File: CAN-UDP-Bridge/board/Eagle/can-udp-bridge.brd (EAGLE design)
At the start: 23.8 x 35.5 mm, 15 parts, among them IC2 MCP1703DB, Q1 16M, X1 B4B-ZR

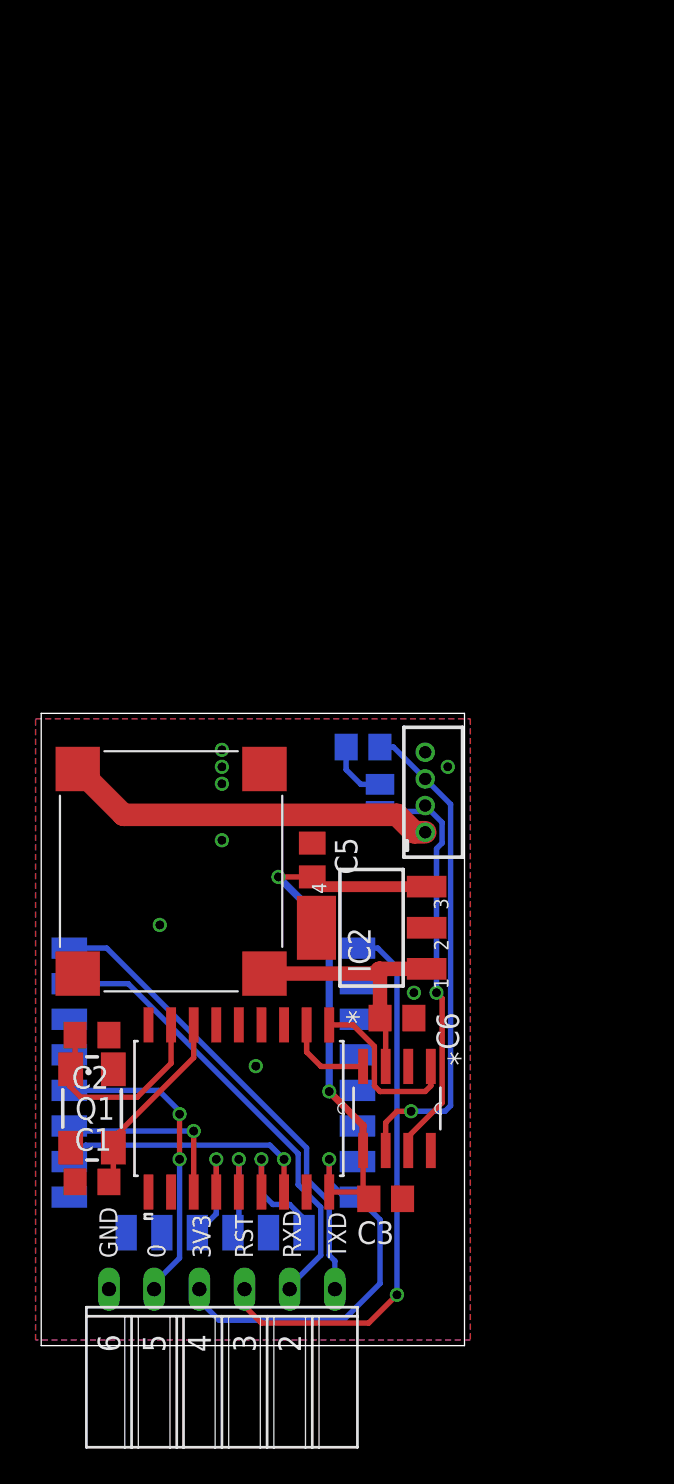
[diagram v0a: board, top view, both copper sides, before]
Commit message: Schnittstelle angepasst an FT232RL.
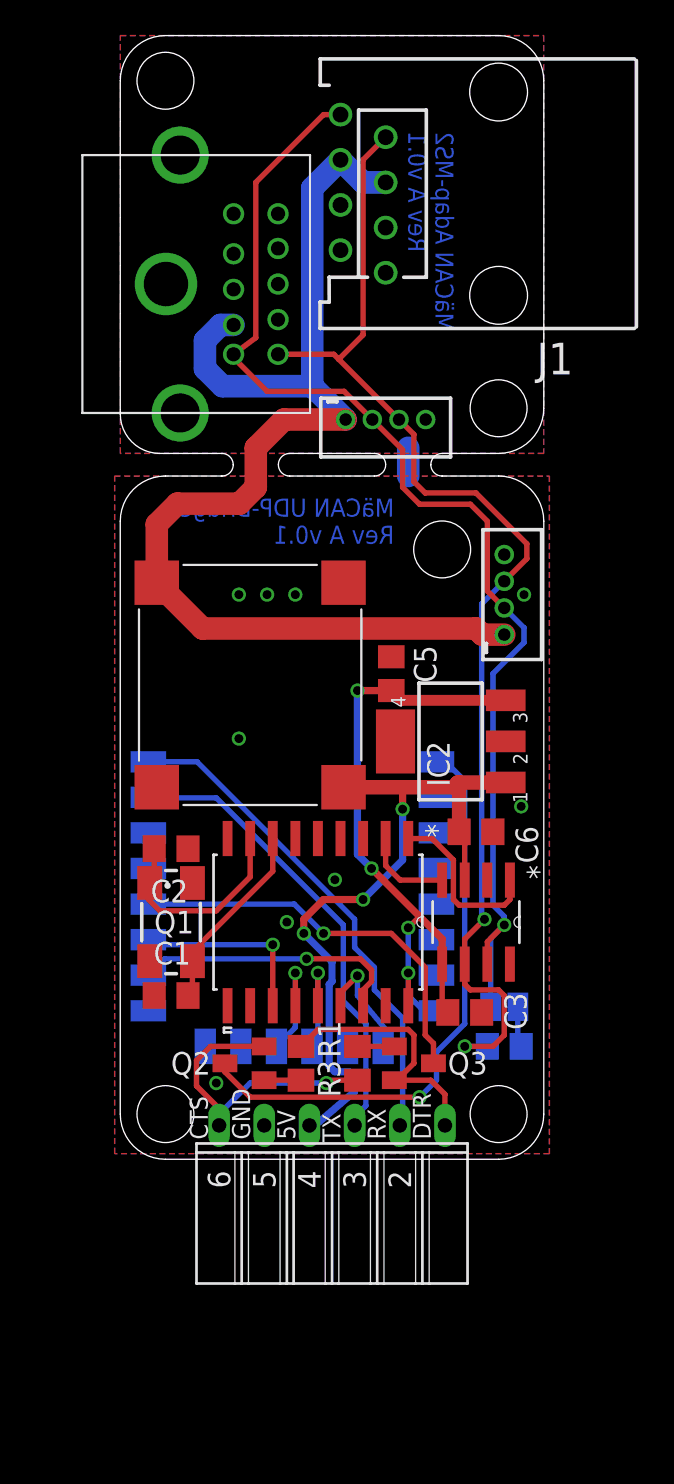
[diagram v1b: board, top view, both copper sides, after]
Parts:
- added J1: (no value), con-amp:215877-7
- added Q2, Q3: (no value), semicon-smd-ipc:SOT23
- added R1, R3: 12k, rcl:R0805
- added U$4: MARKLIN-MD-10, Marklin-Mini-DIN:MARKLIN-MD-10-PRINT
- added X3: B4B-ZR, con-jst:B4B-ZR
- moved R2 18.6 mm to (26.7, 16.8), turned to 180 degrees
- moved CAN-TERM 13.7 mm to (26.7, 19.1), turned to 180 degrees
- moved X1 12.0 mm to (26.7, 42.2)
- moved C2 11.4 mm to (7.94, 27.9)
- moved C3 11.4 mm to (24.4, 18.7)
- moved MDL1 11.4 mm to (22.9, 16.8)
- moved C1 11.4 mm to (7.94, 19.7)
- moved C5 11.4 mm to (20.3, 37.8)
- moved C6 11.4 mm to (25.1, 28.9)
- moved Q1 11.4 mm to (7.94, 23.8)
- moved U$1 11.4 mm to (16.2, 23.8)
- moved U$2 11.4 mm to (25.1, 23.8)
- moved U$3 11.4 mm to (12.4, 37.1)
- moved IC2 11.4 mm to (23.7, 34.0)
- moved PROG 11.1 mm to (17.0, 12.4)
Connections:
- new net DTR: PROG.1, Q3.2, R3.1
- new net N$12: Q2.1, R3.2
- new net N$16: MDL1.16, PROG.2
- new net N$17: MDL1.15, PROG.3
- net +18V: now also J1.5, J1.6, U$4.1, X3.1
- net +3V3: no longer PROG.4
- net +5V: now also PROG.4
- net CAN_H: now also J1.8, U$4.4, X3.2
- net CAN_L: now also J1.7, U$4.8, X3.3
- net GND: now also J1.3, J1.4, PROG.5, U$4.2, U$4.GND1, U$4.GND2, U$4.GND3, X3.4; no longer PROG.6
- net N$10: now also MDL1.12, Q3.3; no longer MDL1.1, PROG.3
- net N$11: now also Q3.1, R1.2; no longer MDL1.12, PROG.5
- net N$3: now also PROG.6, Q2.2, R1.1; no longer MDL1.16, PROG.1
- net N$4: now also MDL1.1, Q2.3; no longer MDL1.15, PROG.2
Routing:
- net +18V: track 21.0 -> 67.5 mm
- net CAN_H: track 23.5 -> 68.2 mm
- net CAN_L: track 27.9 -> 68.3 mm, vias 1 -> 2
- net N$16: track 0.00 -> 28.0 mm
- net N$17: track 0.00 -> 26.0 mm
- net +5V: track 14.8 -> 40.6 mm, vias 0 -> 3
- net +3V3: track 53.8 -> 37.9 mm, vias 3 -> 4
- net N$11: track 17.3 -> 2.07 mm, vias 2 -> 0
- net DTR: track 0.00 -> 14.7 mm
- net N$3: track 26.6 -> 17.5 mm, vias 0 -> 1
- net N$10: track 31.7 -> 22.6 mm
- net N$4: track 25.7 -> 32.9 mm, vias 0 -> 1
- net N$12: track 0.00 -> 2.08 mm
- net GND: track 0.00 -> 1.59 mm, vias 8 -> 9
- net N$15: track 3.52 -> 2.30 mm
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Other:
- board size 23.8 x 35.5 mm -> 23.8 x 63.2 mm
- board text added: "5V"
- board text added: "CTS"
- board text added: "DTR"
- board text added: "MäCAN Adap-MS2 Rev A v0.1"
- board text added: "MäCAN UDP-Bridge Rev A v0.1"
- board text added: "RX"
- board text added: "TX"
- board text removed: "0"
- board text removed: "3V3"
- board text removed: "RST"
- board text removed: "RXD"
- board text removed: "TXD"

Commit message: Schnittstelle angepasst an FT232RL.
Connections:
- net +5V: no longer PROG.4
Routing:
- net +5V: track 40.6 -> 14.8 mm, vias 3 -> 0
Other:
- board text added: "VIN"
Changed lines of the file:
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@@
 <text x="10.00125" y="11.58875" size="1.016" layer="25" rot="R90">CTS</text>
 <text x="12.3825" y="11.58875" size="1.016" layer="25" rot="R90">GND</text>
-<text x="14.9225" y="11.58875" size="1.016" layer="25" rot="R90">5V</text>
+<text x="18.89125" y="30.1625" size="1.016" layer="25">5V</text>
 <text x="17.4625" y="11.43" size="1.016" layer="25" rot="R90">TX</text>
 <text x="20.0025" y="11.58875" size="1.016" layer="25" rot="R90">RX</text>
@@
 <wire x1="28.8925" y1="13.0175" x2="28.8925" y2="46.355" width="0" layer="20"/>
 <wire x1="5.08" y1="46.355" x2="7.62" y2="48.895" width="0" layer="20" curve="-90"/>
+<text x="16.35125" y="44.45" size="1.016" layer="25">GND</text>
+<text x="16.35125" y="44.45" size="1.016" layer="25">GND</text>
+<text x="5.87375" y="44.45" size="1.016" layer="25">VIN</text>
 </plain>
 <attributes>
@@
 <via x="14.44625" y="23.8125" extent="1-16" drill="0.5" diameter="0.254"/>
 <via x="10.4775" y="14.76375" extent="1-16" drill="0.5" diameter="0.254"/>
-<wire x1="6.66" y1="18.8275" x2="6.9875" y2="19.685" width="0" layer="19" extent="1-16"/>
 </signal>
 <signal name="+3V3">
@@
 <wire x1="24.1325" y1="28.8925" x2="24.1325" y2="31.6586" width="0.8128" layer="1"/>
 <wire x1="24.1325" y1="31.6586" x2="24.13" y2="31.6611" width="0.8128" layer="1"/>
-<wire x1="17.6325" y1="31.3975" x2="20.955" y2="31.3975" width="0.8128" layer="1"/>
-<wire x1="20.955" y1="31.3975" x2="23.7775" y2="31.3975" width="0.8128" layer="1"/>
+<wire x1="17.6325" y1="31.3975" x2="23.7775" y2="31.3975" width="0.8128" layer="1"/>
 <wire x1="24.13" y1="31.6611" x2="24.0411" y2="31.6611" width="0.8128" layer="1"/>
 <wire x1="24.0411" y1="31.6611" x2="23.7775" y2="31.3975" width="0.8128" layer="1"/>
-<contactref element="PROG" pad="4"/>
-<wire x1="15.71625" y1="12.3825" x2="16.03375" y2="12.3825" width="0.4064" layer="16"/>
-<wire x1="16.03375" y1="12.3825" x2="18.25625" y2="14.2875" width="0.4064" layer="16"/>
-<wire x1="18.25625" y1="14.2875" x2="18.25625" y2="15.08125" width="0.4064" layer="16"/>
-<wire x1="16.98625" y1="21.59" x2="15.39875" y2="23.1775" width="0.4064" layer="16"/>
-<via x="15.39875" y="23.1775" extent="1-16" drill="0.5" diameter="0.254"/>
-<wire x1="15.39875" y1="23.1775" x2="15.39875" y2="23.97125" width="0.4064" layer="1"/>
-<wire x1="15.39875" y1="23.97125" x2="16.51" y2="25.0825" width="0.4064" layer="1"/>
-<wire x1="16.51" y1="25.0825" x2="18.7325" y2="25.0825" width="0.4064" layer="1"/>
-<via x="18.7325" y="25.0825" extent="1-16" drill="0.5" diameter="0.254"/>
-<wire x1="18.7325" y1="25.0825" x2="20.955" y2="27.305" width="0.4064" layer="16"/>
-<wire x1="20.955" y1="27.305" x2="20.955" y2="30.1625" width="0.4064" layer="16"/>
-<via x="20.955" y="30.1625" extent="1-16" drill="0.5" diameter="0.254"/>
-<wire x1="20.955" y1="30.1625" x2="20.955" y2="31.3975" width="0.4064" layer="1"/>
-<wire x1="18.25625" y1="15.08125" x2="17.93875" y2="15.39875" width="0.4064" layer="16"/>
-<wire x1="17.93875" y1="15.39875" x2="17.145" y2="15.39875" width="0.4064" layer="16"/>
-<wire x1="17.145" y1="15.39875" x2="16.8275" y2="15.71625" width="0.4064" layer="16"/>
-<wire x1="16.98625" y1="21.59" x2="16.98625" y2="20.47875" width="0.4064" layer="16"/>
-<wire x1="16.98625" y1="20.47875" x2="16.8275" y2="20.32" width="0.4064" layer="16"/>
-<wire x1="16.8275" y1="20.32" x2="16.8275" y2="15.71625" width="0.4064" layer="16"/>
 </signal>
 <signal name="+18V">
@@
 <wire x1="18.89125" y1="18.0975" x2="17.62125" y2="19.3675" width="0.3048" layer="16"/>
 <wire x1="17.62125" y1="19.3675" x2="17.62125" y2="23.65375" width="0.3048" layer="16"/>
+<wire x1="10.4775" y1="30.7975" x2="6.69" y2="30.7975" width="0.3048" layer="16"/>
 <wire x1="17.62125" y1="23.65375" x2="10.4775" y2="30.7975" width="0.3048" layer="16"/>
-<wire x1="10.4775" y1="30.7975" x2="6.69" y2="30.7975" width="0.3048" layer="16"/>
 <wire x1="6.69" y1="30.7975" x2="6.66" y2="30.8275" width="0.3048" layer="16"/>
 </signal>

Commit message: Add files via upload
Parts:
- added TRACK: (no value), jumper:JP1
- U$2: value MCP2551-E/SN -> MCP2562
- renumbered PROG to PROG/TTL
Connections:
- new net N$18: J1.2, TRACK.2
- new net N$19: J1.1, TRACK.1
- net +3V3: now also MDL1.3
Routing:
- net N$18: track 0.00 -> 7.53 mm
- net N$19: track 0.00 -> 6.26 mm
- net +3V3: track 37.9 -> 42.3 mm
- net CAN_H: track 68.2 -> 67.2 mm
- net +18V: track 67.5 -> 66.8 mm
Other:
- board text added: "MäCAN Adap Rev A v0.1"
- board text added: "b"
- board text added: "r"
- board text removed: "MäCAN Adap-MS2 Rev A v0.1"

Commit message: Add files via upload
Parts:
- added C4, C7: 100n, rcl:C0805
- added R4: 12k, rcl:R0805
- moved C3 3.43 mm to (27.3, 16.8), turned to 90 degrees
- moved CAN-TERM 2.56 mm to (26.4, 21.6)
- moved C6 0.79 mm to (25.1, 29.7)
- moved PROG/TTL 0.64 mm to (17.6, 12.4)
- moved R2 0.63 mm to (26.7, 17.5), turned to 90 degrees
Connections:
- new net N$20: R4.2, U$1.17
- net +18V: no longer J1.5
- net +3V3: now also C4.2, R4.1
- net +5V: now also C7.1
- net GND: now also C4.1, C7.2; no longer J1.3
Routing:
- net N$20: track 0.00 -> 12.1 mm
- net +5V: track 14.8 -> 25.0 mm, vias 0 -> 1
- net +3V3: track 42.3 -> 51.8 mm
- net CAN_H: track 67.2 -> 63.3 mm
- net CAN_L: track 68.3 -> 64.9 mm
- net N$4: track 32.9 -> 35.7 mm
- net N$7: track 6.11 -> 8.88 mm
- net N$9: track 6.41 -> 9.00 mm
- net +18V: track 66.8 -> 64.4 mm
- net N$8: track 10.5 -> 9.24 mm
- net N$15: track 2.30 -> 3.47 mm
- net N$6: track 15.4 -> 14.5 mm
- net N$5: track 6.68 -> 6.13 mm
- net N$10: vias 1 -> 3
- net GND: vias 9 -> 11
